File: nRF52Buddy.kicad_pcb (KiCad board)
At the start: 4 copper layers, 60 x 35 mm, 94 parts, among them J1 2060-452_998-404, J2 SWD, J3 2305018-2, J4 Conn_02x26_Odd_Even, J5 Conn_02x26_Odd_Even, J6 HDGC1251WR-S-2P, Q1 SSM3J332R, Q2 SSM3J332R, Q3 SSM3J332R, SW1 SW_SPST, U1 AP9211, U2 MAX17260SETD, U3 TP4054, U4 TP6841S6, U5 MIC5205-3.3YM5, U6 MDBT50Q-1MV2, U7 USBLC6-2SC6, Y1 32.768 kHz

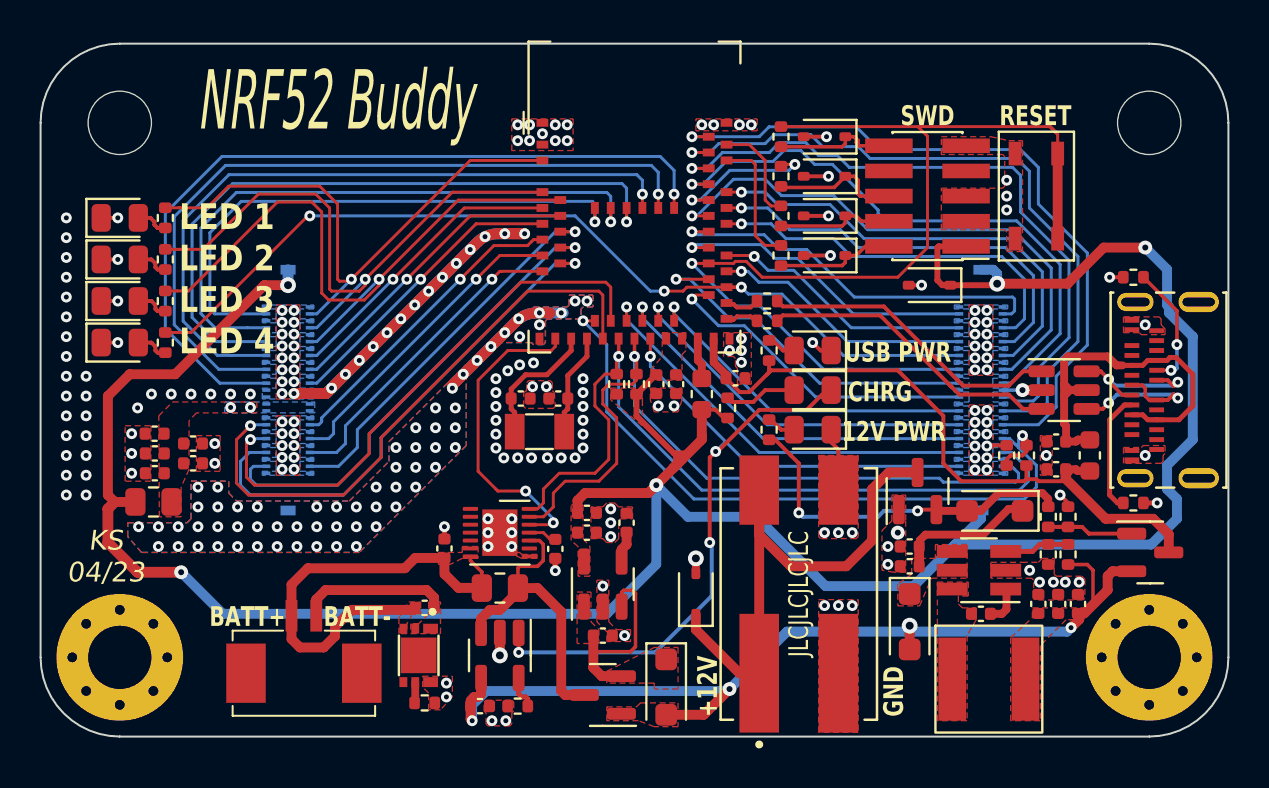
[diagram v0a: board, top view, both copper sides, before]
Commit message: changed LED net names to indicate status LEDs and changed 3V3 pin on mezzanine connector to be GND
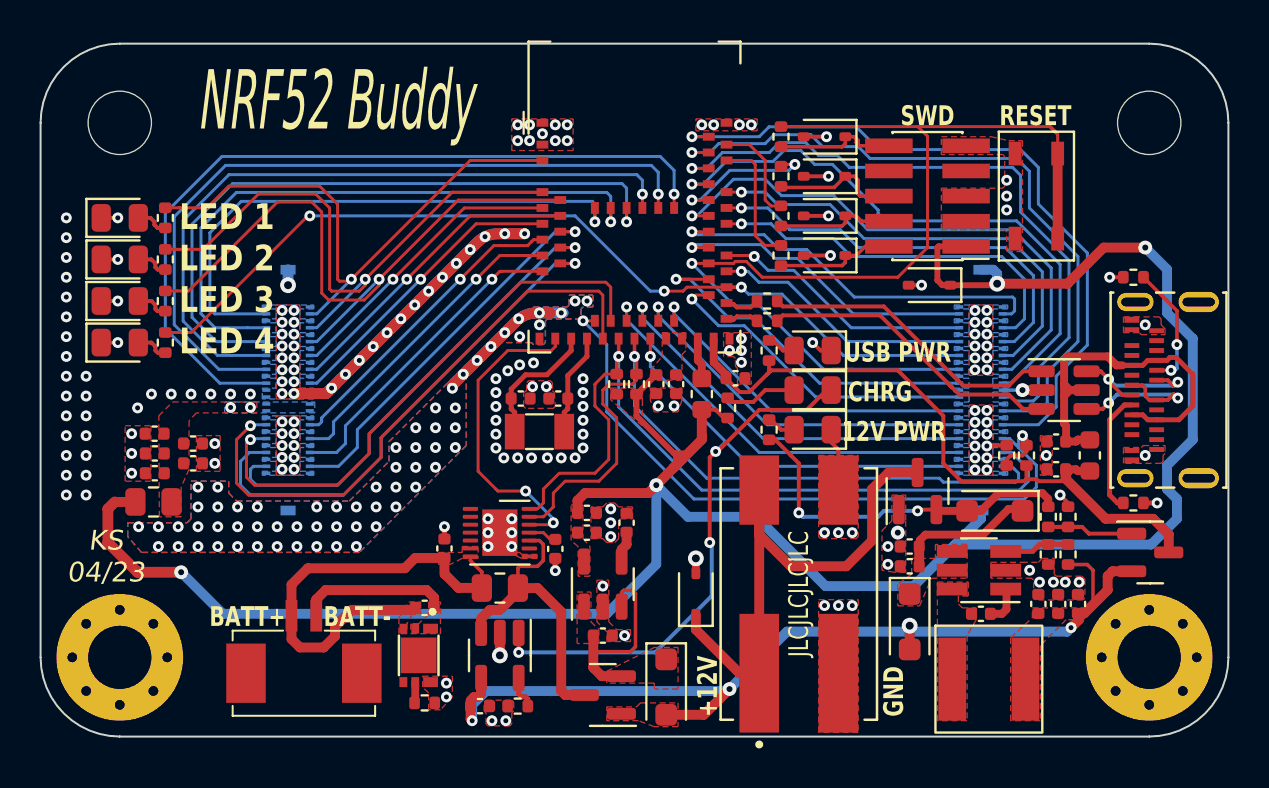
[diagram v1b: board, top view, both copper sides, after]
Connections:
- net /Connectors/P1.10 renamed /Connectors/P1.10/STATUS_LED1
- net /Connectors/P1.11 renamed /Connectors/P1.11/STATUS_LED2
- net /Connectors/P1.12 renamed /Connectors/P1.12/STATUS_LED3
- net /MCU (nRF52840)/P0.13/BT_STATUS_LED renamed /MCU (nRF52840)/P0.13/STATUS_LED4
- J5 pad 52: +3V3 -> GND
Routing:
- net +3V3: track 137.5 -> 119.8 mm, vias 5 -> 4
- net GND: track 69.6 -> 70.4 mm, vias 255 -> 256
